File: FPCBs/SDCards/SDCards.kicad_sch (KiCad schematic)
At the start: 4 parts, among them J1 SD_Card_Device, J2 SD_Card_Device, J3 SD_Card_Device, J4 SD_Card_Device

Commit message: sd card
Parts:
- J1, J2, J3, J4: symbol Connector:SD_Card_Device -> Leica-G9ii-Symbols:SD_Card_UHS2
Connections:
- net at J1.3 (VSS1), J2.3 (VSS1): no longer J1.6 (VSS), J2.6 (VSS)
- net at J3.3 (VSS1), J4.3 (VSS1): no longer J3.6 (VSS), J4.6 (VSS)
- new net: J1.10 (VSS3), J2.10 (VSS3)
- new net: J1.11 (D0+), J2.11 (D0+)
- new net: J1.12 (D0-), J2.12 (D0-)
- new net: J1.13 (VSS4), J2.13 (VSS4)
- new net: J1.14 (VDD2), J2.14 (VDD2)
- new net: J1.15 (D1-), J2.15 (D1-)
- new net: J1.16 (D1+), J2.16 (D1+)
- new net: J1.17 (Name), J2.17 (Name)
- new net: J1.6 (VSS2), J2.6 (VSS2)
- new net: J3.10 (VSS3), J4.10 (VSS3)
- new net: J3.11 (D0+), J4.11 (D0+)
- new net: J3.12 (D0-), J4.12 (D0-)
- new net: J3.13 (VSS4), J4.13 (VSS4)
- new net: J3.14 (VDD2), J4.14 (VDD2)
- new net: J3.15 (D1-), J4.15 (D1-)
- new net: J3.16 (D1+), J4.16 (D1+)
- new net: J3.17 (Name), J4.17 (Name)
- new net: J3.6 (VSS2), J4.6 (VSS2)

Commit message: Fix sd card
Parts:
- J1, J3: footprint Leica-G9ii:SD_Card_Socket_UHS-II_HTK_AXA573062 -> Leica-G9ii:SD_Card_Socket_UHS-II_Extender; symbol Leica-G9ii-Symbols:SD_Card_UHS2 -> Leica-G9ii-Symbols:SD_Card_Socket_UHS2
- J2, J4: symbol Leica-G9ii-Symbols:SD_Card_UHS2 -> Leica-G9ii-Symbols:SD_Card_Socket_UHS2
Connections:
- net at J1.10 (VSS3), J2.10 (VSS3): now also J1.3 (VSS1), J2.3 (VSS1)
- new net: J1.CD (CARD_DETECT), J1.COM (COMMON), J1.WP (WRITE_PROTECT)
- new net: J3.CD (CARD_DETECT), J4.CD (CARD_DETECT)
- new net: J3.COM (COMMON), J4.COM (COMMON)
- new net: J3.WP (WRITE_PROTECT), J4.WP (WRITE_PROTECT)
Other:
- note added: "SD1 - external"
- note added: "SD2 - internal soldered"
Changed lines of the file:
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@@
 	(generator_version "9.0")
 	(paper "A4")
+	(text "SD1 - external"
+		(exclude_from_sim no)
+		(at 195.58 133.096 0)
+		(effects
+			(font
+				(size 1.27 1.27)
+			)
+		)
+	)
+	(text "SD2 - internal soldered"
+		(exclude_from_sim no)
+		(at 197.612 57.404 0)
+		(effects
+			(font
+				(size 1.27 1.27)
+			)
+		)
+	)
+	(junction
+		(at 105.41 33.02)
+		(diameter 0)
+		(color 0 0 0 0)
+	)
+	(junction
+		(at 105.41 67.31)
+		(diameter 0)
+		(color 0 0 0 0)
+	)
+	(junction
+		(at 66.04 85.09)
+		(diameter 0)
+		(color 0 0 0 0)
+	)
+	(wire
+		(pts
+			(xy 105.41 33.02) (xy 105.41 67.31)
+		)
+		(stroke
+			(width 0)
+			(type default)
+		)
+	)
+	(wire
+		(pts
+			(xy 50.8 81.28) (xy 50.8 85.09)
+		)
+		(stroke
+			(width 0)
+			(type default)
+		)
+	)
 	(wire
 		(pts
@@
 	(wire
 		(pts
+			(xy 50.8 161.29) (xy 50.8 156.21)
+		)
+		(stroke
+			(width 0)
+			(type default)
+		)
+	)
+	(wire
+		(pts
 			(xy 29.21 26.67) (xy 29.21 67.31)
 		)
@@
 	(wire
 		(pts
+			(xy 48.26 156.21) (xy 48.26 162.56)
+		)
+		(stroke
+			(width 0)
+			(type default)
+		)
+	)
+	(wire
+		(pts
 			(xy 83.82 125.73) (xy 116.84 125.73)
 		)
@@
 	(wire
 		(pts
+			(xy 149.86 161.29) (xy 50.8 161.29)
+		)
+		(stroke
+			(width 0)
+			(type default)
+		)
+	)
+	(wire
+		(pts
 			(xy 170.18 26.67) (xy 29.21 26.67)
 		)
@@
 	(wire
 		(pts
-			(xy 35.56 33.02) (xy 163.83 33.02)
-		)
-		(stroke
-			(width 0)
-			(type default)
-		)
-	)
-	(wire
-		(pts
-			(xy 83.82 67.31) (xy 115.57 67.31)
+			(xy 35.56 33.02) (xy 105.41 33.02)
+		)
+		(stroke
+			(width 0)
+			(type default)
+		)
+	)
+	(wire
+		(pts
+			(xy 83.82 67.31) (xy 105.41 67.31)
+		)
+		(stroke
+			(width 0)
+			(type default)
+		)
+	)
+	(wire
+		(pts
+			(xy 134.62 160.02) (xy 134.62 156.21)
+		)
+		(stroke
+			(width 0)
+			(type default)
+		)
+	)
+	(wire
+		(pts
+			(xy 66.04 87.63) (xy 66.04 85.09)
 		)
 		(stroke
@@
 	(wire
 		(pts
+			(xy 105.41 67.31) (xy 115.57 67.31)
+		)
+		(stroke
+			(width 0)
+			(type default)
+		)
+	)
+	(wire
+		(pts
 			(xy 33.02 129.54) (xy 36.83 129.54)
 		)
@@
 	(wire
 		(pts
+			(xy 48.26 162.56) (xy 152.4 162.56)
+		)
+		(stroke
+			(width 0)
+			(type default)
+		)
+	)
+	(wire
+		(pts
 			(xy 31.75 59.69) (xy 36.83 59.69)
 		)
@@
 	(wire
 		(pts
+			(xy 66.04 156.21) (xy 66.04 160.02)
+		)
+		(stroke
+			(width 0)
+			(type default)
+		)
+	)
+	(wire
+		(pts
 			(xy 83.82 45.72) (xy 115.57 45.72)
 		)
@@
 	(wire
 		(pts
+			(xy 48.26 81.28) (xy 48.26 87.63)
+		)
+		(stroke
+			(width 0)
+			(type default)
+		)
+	)
+	(wire
+		(pts
 			(xy 173.99 97.79) (xy 173.99 149.86)
 		)
@@
 	(wire
 		(pts
+			(xy 66.04 160.02) (xy 134.62 160.02)
+		)
+		(stroke
+			(width 0)
+			(type default)
+		)
+	)
+	(wire
+		(pts
+			(xy 152.4 162.56) (xy 152.4 156.21)
+		)
+		(stroke
+			(width 0)
+			(type default)
+		)
+	)
+	(wire
+		(pts
 			(xy 34.29 127) (xy 34.29 105.41)
 		)
@@
 	(wire
 		(pts
+			(xy 50.8 85.09) (xy 66.04 85.09)
+		)
+		(stroke
+			(width 0)
+			(type default)
+		)
+	)
+	(wire
+		(pts
 			(xy 168.91 102.87) (xy 168.91 134.62)
 		)
@@
 	(wire
 		(pts
+			(xy 149.86 156.21) (xy 149.86 161.29)
+		)
+		(stroke
+			(width 0)
+			(type default)
+		)
+	)
+	(wire
+		(pts
 			(xy 83.82 123.19) (xy 116.84 123.19)
 		)
@@
 	(wire
 		(pts
+			(xy 48.26 87.63) (xy 66.04 87.63)
+		)
+		(stroke
+			(width 0)
+			(type default)
+		)
+	)
+	(wire
+		(pts
 			(xy 172.72 99.06) (xy 27.94 99.06)
 		)
@@
 	(wire
 		(pts
+			(xy 105.41 33.02) (xy 163.83 33.02)
+		)
+		(stroke
+			(width 0)
+			(type default)
+		)
+	)
+	(wire
+		(pts
+			(xy 66.04 81.28) (xy 66.04 85.09)
+		)
+		(stroke
+			(width 0)
+			(type default)
+		)
+	)
+	(wire
+		(pts
 			(xy 26.67 24.13) (xy 26.67 74.93)
 		)
@@
 	)
 	(symbol
-		(lib_id "Leica-G9ii-Symbols:SD_Card_UHS2")
+		(lib_id "Leica-G9ii-Symbols:SD_Card_Socket_UHS2")
 		(at 60.96 60.96 0)
 		(mirror y)
@@
 			)
 		)
-		(property "Footprint" "Leica-G9ii:SD_Card_Socket_UHS-II_HTK_AXA573062"
+		(property "Footprint" "Leica-G9ii:SD_Card_Socket_UHS-II_Extender"
 			(at 52.07 64.262 0)
 			(effects
@@
 			)
 		)
-		(property "Datasheet" "http://www.convict.lu/pdf/ProdManualSDCardv1.9.pdf"
+		(property "Datasheet" ""
 			(at 61.468 92.202 0)
 			(effects
@@
 		)
 		(pin "13"
+		)
+		(pin "WP"
+		)
+		(pin "COM"
+		)
+		(pin "CD"
 		)
 		(instances
@@
 	)
 	(symbol
-		(lib_id "Leica-G9ii-Symbols:SD_Card_UHS2")
+		(lib_id "Leica-G9ii-Symbols:SD_Card_Socket_UHS2")
 		(at 139.7 135.89 0)
 		(unit 1)
@@
 		(pin "12"
 		)
+		(pin "WP"
+		)
+		(pin "CD"
+		)
+		(pin "COM"
+		)
 		(instances
 			(project "SDCards"
@@
 	)
 	(symbol
-		(lib_id "Leica-G9ii-Symbols:SD_Card_UHS2")
+		(lib_id "Leica-G9ii-Symbols:SD_Card_Socket_UHS2")
 		(at 60.96 135.89 0)
 		(mirror y)
@@
 			)
 		)
-		(property "Footprint" "Leica-G9ii:SD_Card_Socket_UHS-II_HTK_AXA573062"
+		(property "Footprint" "Leica-G9ii:SD_Card_Socket_UHS-II_Extender"
 			(at 52.07 139.192 0)
 			(effects
@@
 			)
 		)
-		(property "Datasheet" "http://www.convict.lu/pdf/ProdManualSDCardv1.9.pdf"
+		(property "Datasheet" ""
 			(at 61.468 167.132 0)
 			(effects
@@
 		)
 		(pin "12"
+		)
+		(pin "COM"
+		)
+		(pin "WP"
+		)
+		(pin "CD"
 		)
 		(instances
@@
 	)
 	(symbol
-		(lib_id "Leica-G9ii-Symbols:SD_Card_UHS2")
+		(lib_id "Leica-G9ii-Symbols:SD_Card_Socket_UHS2")
 		(at 138.43 60.96 0)
 		(unit 1)
@@
 		(pin "16"
 		)
+		(pin "COM"
+		)
+		(pin "WP"
+		)
+		(pin "CD"
+		)
 		(instances

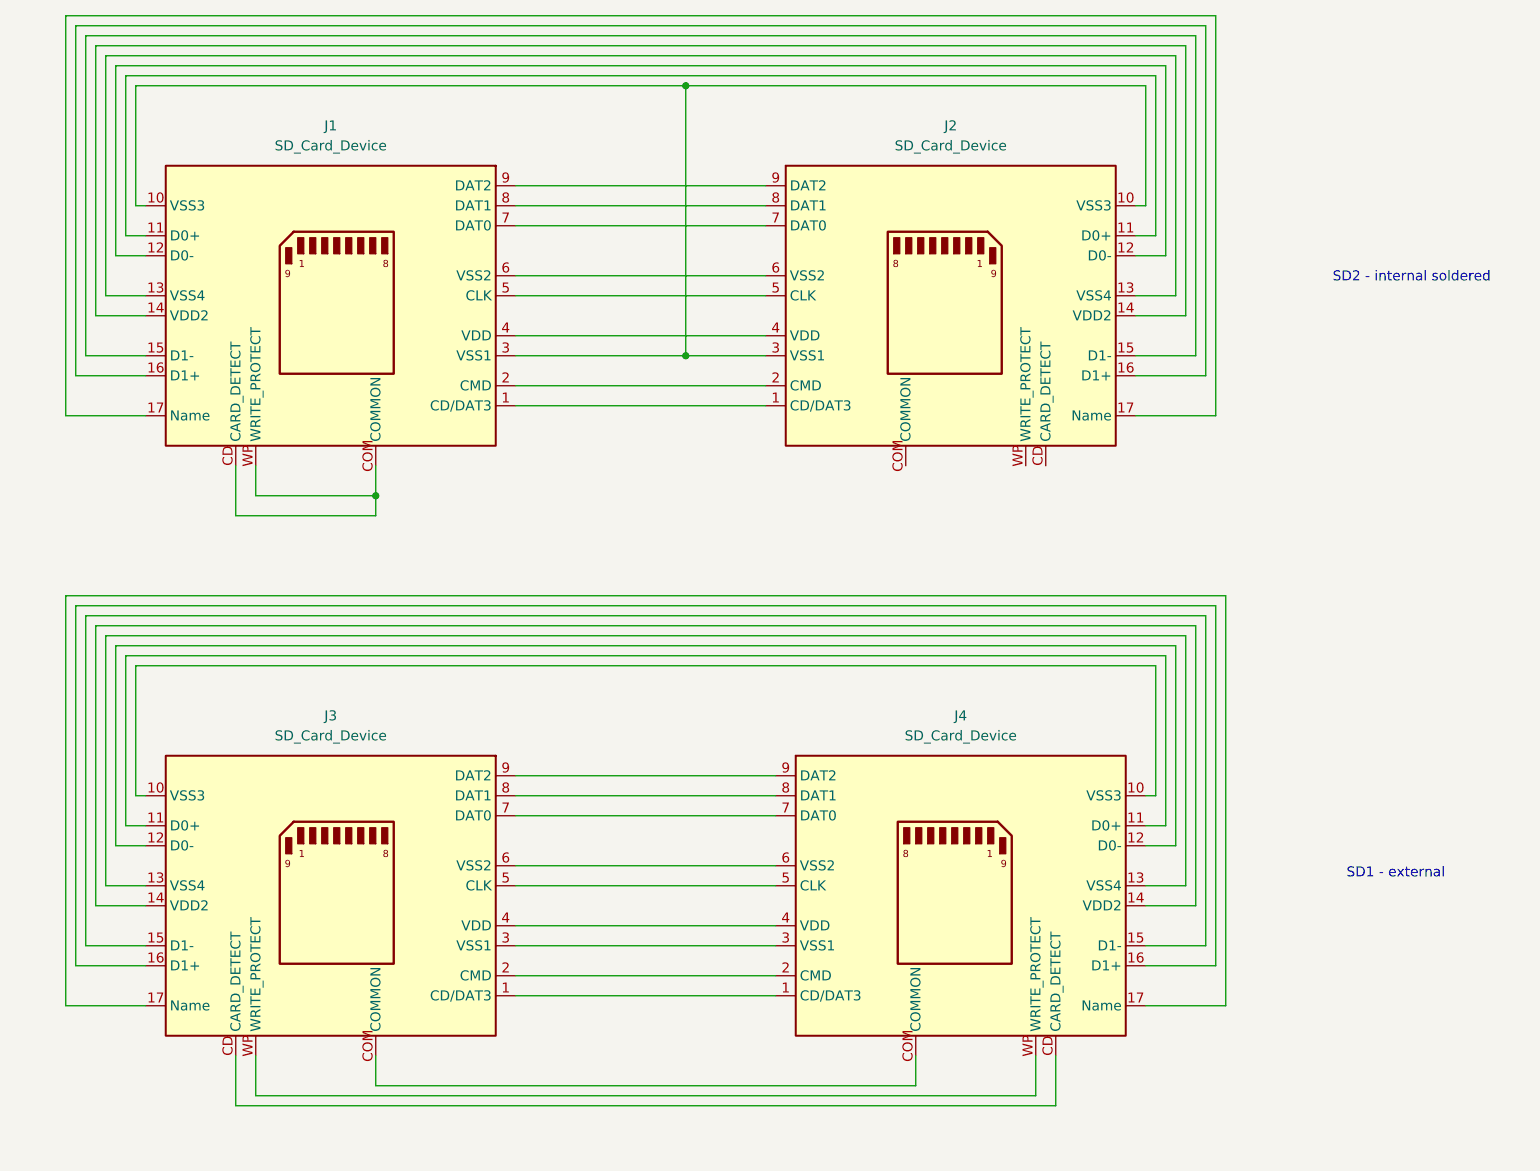
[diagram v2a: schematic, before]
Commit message: Fix spacings and pads
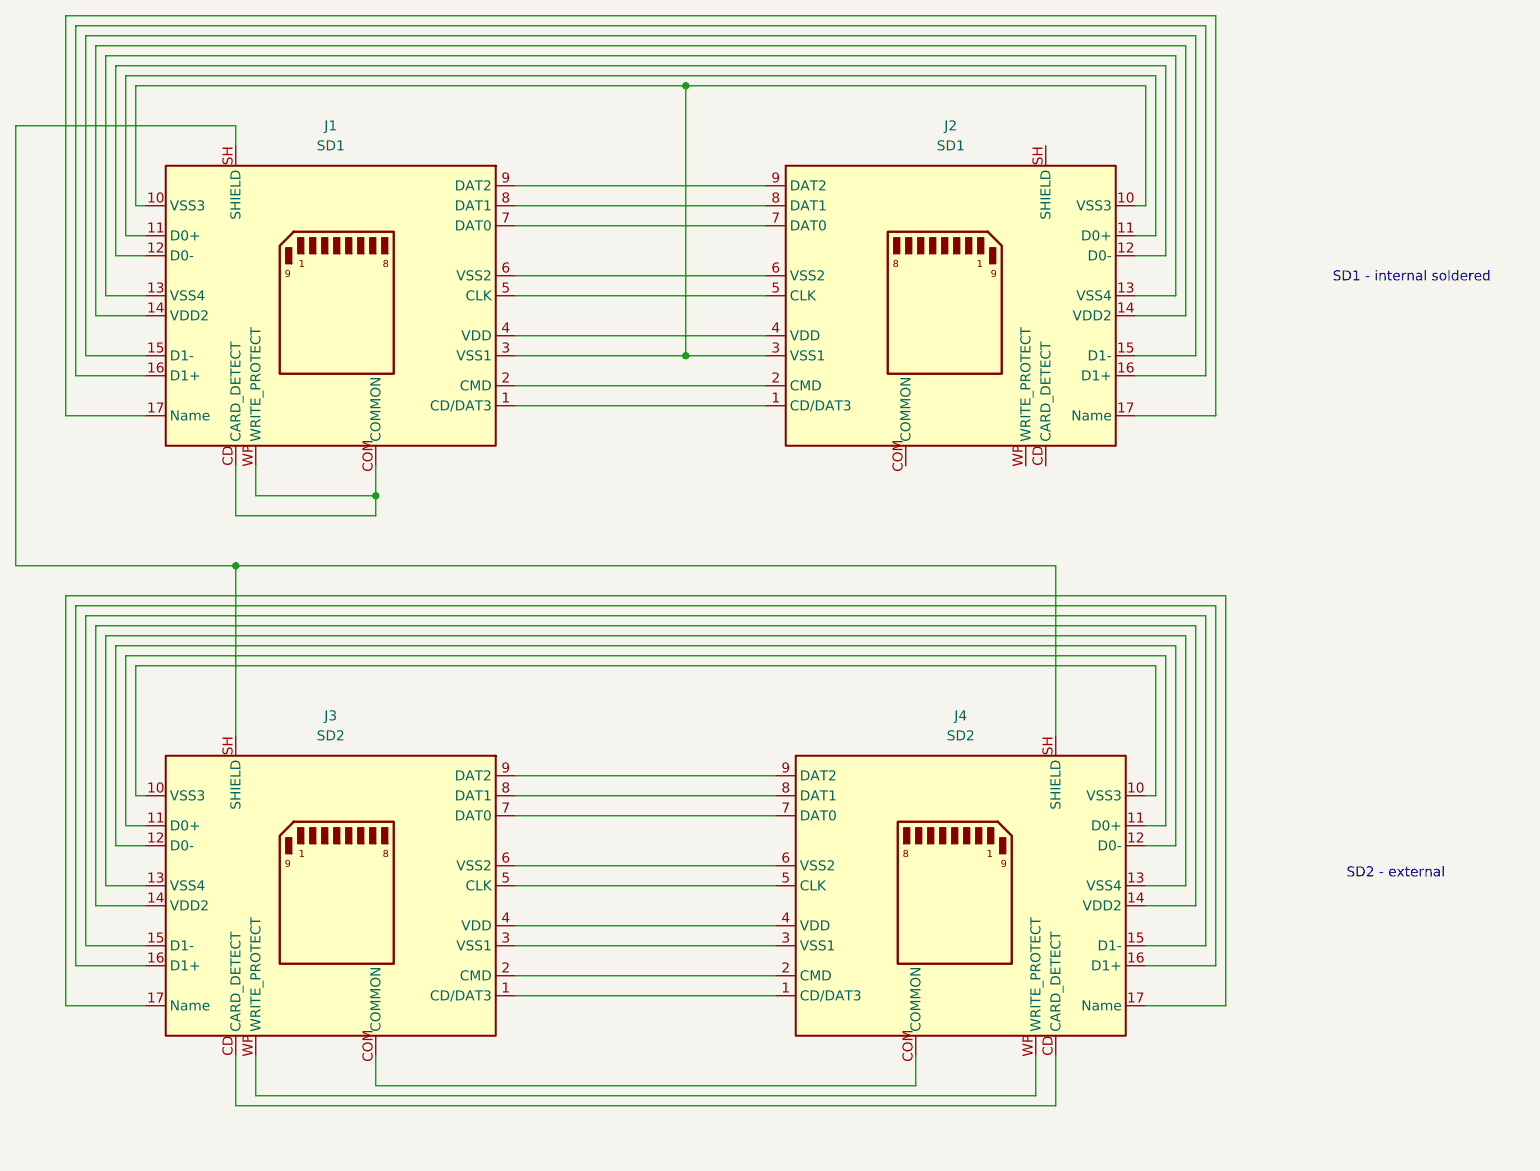
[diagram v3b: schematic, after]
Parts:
- J1, J2: value SD_Card_Device -> SD1
- J3, J4: value SD_Card_Device -> SD2
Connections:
- new net: J1.SH (SHIELD), J3.SH (SHIELD), J4.SH (SHIELD)
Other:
- note added: "SD1 - internal soldered"
- note added: "SD2 - external"
- note removed: "SD1 - external"
- note removed: "SD2 - internal soldered"
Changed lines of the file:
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@@
 	(generator_version "9.0")
 	(paper "A4")
-	(text "SD1 - external"
+	(text "SD2 - external"
 		(exclude_from_sim no)
 		(at 195.58 133.096 0)
@@
 		)
 	)
-	(text "SD2 - internal soldered"
+	(text "SD1 - internal soldered"
 		(exclude_from_sim no)
 		(at 197.612 57.404 0)
@@
 	)
 	(junction
+		(at 48.26 93.98)
+		(diameter 0)
+		(color 0 0 0 0)
+	)
+	(junction
 		(at 66.04 85.09)
 		(diameter 0)
@@
 	(wire
 		(pts
+			(xy 48.26 40.64) (xy 48.26 38.1)
+		)
+		(stroke
+			(width 0)
+			(type default)
+		)
+	)
+	(wire
+		(pts
 			(xy 166.37 54.61) (xy 162.56 54.61)
 		)
@@
 	(wire
 		(pts
+			(xy 48.26 93.98) (xy 152.4 93.98)
+		)
+		(stroke
+			(width 0)
+			(type default)
+		)
+	)
+	(wire
+		(pts
 			(xy 163.83 129.54) (xy 167.64 129.54)
 		)
@@
 	(wire
 		(pts
+			(xy 48.26 93.98) (xy 48.26 115.57)
+		)
+		(stroke
+			(width 0)
+			(type default)
+		)
+	)
+	(wire
+		(pts
 			(xy 170.18 26.67) (xy 29.21 26.67)
 		)
@@
 	(wire
 		(pts
+			(xy 20.32 38.1) (xy 20.32 93.98)
+		)
+		(stroke
+			(width 0)
+			(type default)
+		)
+	)
+	(wire
+		(pts
 			(xy 152.4 162.56) (xy 152.4 156.21)
 		)
@@
 	(wire
 		(pts
+			(xy 152.4 93.98) (xy 152.4 115.57)
+		)
+		(stroke
+			(width 0)
+			(type default)
+		)
+	)
+	(wire
+		(pts
 			(xy 168.91 102.87) (xy 168.91 134.62)
 		)
@@
 	(wire
 		(pts
+			(xy 20.32 93.98) (xy 48.26 93.98)
+		)
+		(stroke
+			(width 0)
+			(type default)
+		)
+	)
+	(wire
+		(pts
 			(xy 168.91 62.23) (xy 162.56 62.23)
+		)
+		(stroke
+			(width 0)
+			(type default)
+		)
+	)
+	(wire
+		(pts
+			(xy 48.26 38.1) (xy 20.32 38.1)
 		)
 		(stroke
@@
 			)
 		)
-		(property "Value" "SD_Card_Device"
+		(property "Value" "SD1"
 			(at 60.325 40.64 0)
 			(effects
@@
 		)
 		(pin "CD"
+		)
+		(pin "SH"
 		)
 		(instances
@@
 			)
 		)
-		(property "Value" "SD_Card_Device"
+		(property "Value" "SD2"
 			(at 140.335 115.57 0)
 			(effects
@@
 		)
 		(pin "COM"
+		)
+		(pin "SH"
 		)
 		(instances
@@
 			)
 		)
-		(property "Value" "SD_Card_Device"
+		(property "Value" "SD2"
 			(at 60.325 115.57 0)
 			(effects
@@
 		)
 		(pin "CD"
+		)
+		(pin "SH"
 		)
 		(instances
@@
 			)
 		)
-		(property "Value" "SD_Card_Device"
+		(property "Value" "SD1"
 			(at 139.065 40.64 0)
 			(effects
@@
 		(pin "CD"
 		)
+		(pin "SH"
+		)
 		(instances
